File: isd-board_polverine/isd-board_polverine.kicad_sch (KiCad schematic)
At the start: 27 parts, among them J1 BATT, J10 Conn_01x02_Pin, J12 Conn_02x10_Odd_Even, J3 Conn_01x02_Pin, J4 Conn_02x08_Odd_Even, J5 Conn_02x08_Odd_Even, J8 USB_C_Receptacle_PowerOnly_6P, J9 Conn_01x04_Socket, Q1 Q_Dual_NMOS_S1G1D2S2G2D1, U1 DW01A

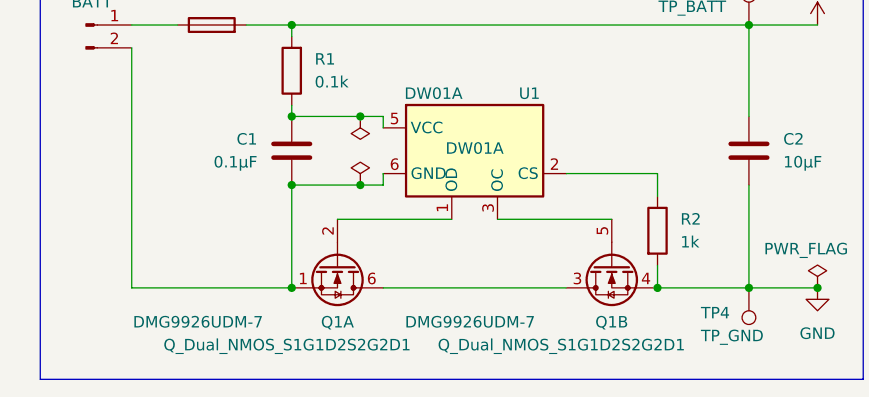
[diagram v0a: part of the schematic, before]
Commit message: update: battery protection circuit (compact placement)
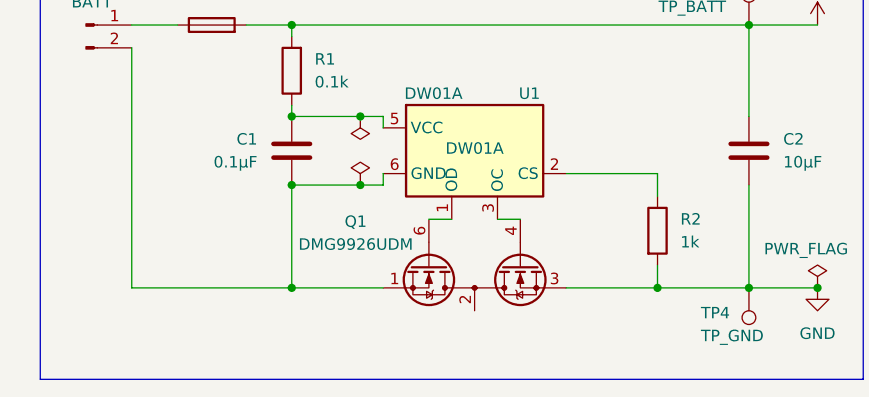
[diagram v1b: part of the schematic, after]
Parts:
- removed Q1: Q_Dual_NMOS_S1G1D2S2G2D1, Package_TO_SOT_SMD:SOT-23-6_Handsoldering, symbol Transistor_FET:Q_Dual_NMOS_S1G1D2S2G2D1
- added Q1: DMG9926UDM, Package_TO_SOT_SMD:SOT-23-6, symbol Transistor_FET:DMG9926UDM
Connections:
- net GND: now also Q1.3 (S2)
- net at U1.1 (OD): now also Q1.6 (G1)
- net at U1.3 (OC): now also Q1.4 (G2)
- net at C1.2, J1.2 (Pin_2), U1.6 (GND): now also Q1.1 (D1)
- new net: Q1.2 (S1/D2), Q1.5 (S1/D2)
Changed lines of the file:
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@@
 	)
 	(junction
-		(at 46.99 152.4)
+		(at 87.63 181.61)
 		(diameter 0)
 		(color 0 0 0 0)
 	)
 	(junction
-		(at 146.05 173.99)
+		(at 46.99 152.4)
 		(diameter 0)
 		(color 0 0 0 0)
 	)
 	(junction
-		(at 139.7 74.93)
+		(at 146.05 173.99)
 		(diameter 0)
 		(color 0 0 0 0)
 	)
 	(junction
-		(at 46.99 181.61)
+		(at 139.7 74.93)
 		(diameter 0)
 		(color 0 0 0 0)
@@
 	)
 	(junction
-		(at 97.79 181.61)
+		(at 46.99 181.61)
 		(diameter 0)
 		(color 0 0 0 0)
 	)
 	(junction
-		(at 62.23 124.46)
+		(at 97.79 181.61)
 		(diameter 0)
 		(color 0 0 0 0)
 	)
 	(junction
-		(at 152.4 107.95)
+		(at 62.23 124.46)
 		(diameter 0)
 		(color 0 0 0 0)
 	)
 	(junction
-		(at 46.99 170.18)
+		(at 152.4 107.95)
 		(diameter 0)
 		(color 0 0 0 0)
 	)
 	(junction
-		(at 87.63 181.61)
+		(at 46.99 170.18)
 		(diameter 0)
 		(color 0 0 0 0)
@@
 	(wire
 		(pts
-			(xy 190.5 83.82) (xy 198.12 83.82)
+			(xy 46.99 181.61) (xy 57.15 181.61)
 		)
 		(stroke
@@
 	(wire
 		(pts
-			(xy 57.15 181.61) (xy 77.47 181.61)
+			(xy 190.5 83.82) (xy 198.12 83.82)
 		)
 		(stroke
@@
 	(wire
 		(pts
-			(xy 69.85 173.99) (xy 82.55 173.99)
-		)
-		(stroke
-			(width 0)
-			(type default)
-		)
-	)
-	(wire
-		(pts
 			(xy 129.54 133.35) (xy 133.35 133.35)
 		)
@@
 	(wire
 		(pts
-			(xy 52.07 173.99) (xy 64.77 173.99)
+			(xy 77.47 181.61) (xy 87.63 181.61)
 		)
 		(stroke
@@
 	(wire
 		(pts
+			(xy 69.85 173.99) (xy 72.39 173.99)
+		)
+		(stroke
+			(width 0)
+			(type default)
+		)
+	)
+	(wire
+		(pts
 			(xy 190.5 86.36) (xy 198.12 86.36)
 		)
@@
 	(wire
 		(pts
+			(xy 62.23 173.99) (xy 64.77 173.99)
+		)
+		(stroke
+			(width 0)
+			(type default)
+		)
+	)
+	(wire
+		(pts
 			(xy 97.79 181.61) (xy 105.41 181.61)
 		)
@@
 	)
 	(symbol
+		(lib_id "Transistor_FET:DMG9926UDM")
+		(at 67.31 181.61 90)
+		(mirror x)
+		(unit 1)
+		(exclude_from_sim no)
+		(in_bom yes)
+		(on_board yes)
+		(dnp no)
+		(property "Reference" "Q1"
+			(at 54.102 174.244 90)
+			(effects
+				(font
+					(size 1.27 1.27)
+				)
+			)
+		)
+		(property "Value" "DMG9926UDM"
+			(at 54.102 176.784 90)
+			(effects
+				(font
+					(size 1.27 1.27)
+				)
+			)
+		)
+		(property "Footprint" "Package_TO_SOT_SMD:SOT-23-6"
+			(at 71.12 184.15 0)
+			(effects
+				(font
+					(size 1.27 1.27)
+					(italic yes)
+				)
+				(justify left)
+				(hide yes)
+			)
+		)
+		(property "Datasheet" "https://www.diodes.com/assets/Datasheets/ds31770.pdf"
+			(at 73.025 184.15 0)
+			(effects
+				(font
+					(size 1.27 1.27)
+				)
+				(justify left)
+				(hide yes)
+			)
+		)
+		(property "Description" "4.2A Id, 20V Vds, Common-Drain, Dual Half Bridge N-Channel MOSFET, 28mOhm Ron, SOT-23-6"
+			(at 67.31 181.61 0)
+			(effects
+				(font
+					(size 1.27 1.27)
+				)
+				(hide yes)
+			)
+		)
+		(pin "5"
+		)
+		(pin "2"
+		)
+		(pin "6"
+		)
+		(pin "3"
+		)
+		(pin "1"
+		)
+		(pin "4"
+		)
+		(instances
+			(project ""
+				(path "/27bbddde-1315-4a7b-91f8-52269d45b0e3"
+					(reference "Q1")
+					(unit 1)
+				)
+			)
+		)
+	)
+	(symbol
 		(lib_id "Device:R")
 		(at 46.99 157.48 180)
@@
 	)
 	(symbol
-		(lib_id "Transistor_FET:Q_Dual_NMOS_S1G1D2S2G2D1")
-		(at 52.07 179.07 270)
-		(unit 1)
-		(exclude_from_sim no)
-		(in_bom yes)
-		(on_board yes)
-		(dnp no)
-		(property "Reference" "Q1"
-			(at 52.07 185.42 90)
-			(effects
-				(font
-					(size 1.27 1.27)
-				)
-			)
-		)
-		(property "Value" "Q_Dual_NMOS_S1G1D2S2G2D1"
-			(at 46.482 187.96 90)
-			(effects
-				(font
-					(size 1.27 1.27)
-				)
-			)
-		)
-		(property "Footprint" "Package_TO_SOT_SMD:SOT-23-6_Handsoldering"
-			(at 52.07 184.15 0)
-			(effects
-				(font
-					(size 1.27 1.27)
-				)
-				(hide yes)
-			)
-		)
-		(property "Datasheet" "https://www.mouser.fi/datasheet/3/175/1/ds31770.pdf"
-			(at 52.07 184.15 0)
-			(effects
-				(font
-					(size 1.27 1.27)
-				)
-				(hide yes)
-			)
-		)
-		(property "Description" "Dual NMOS transistor, 6 pin package"
-			(at 52.07 179.07 0)
-			(effects
-				(font
-					(size 1.27 1.27)
-				)
-				(hide yes)
-			)
-		)
-		(property "MPN" "DMG9926UDM-7"
-			(at 36.576 185.42 90)
-			(effects
-				(font
-					(size 1.27 1.27)
-				)
-			)
-		)
-		(pin "1"
-		)
-		(pin "6"
-		)
-		(pin "4"
-		)
-		(pin "2"
-		)
-		(pin "5"
-		)
-		(pin "3"
-		)
-		(instances
-			(project ""
-				(path "/27bbddde-1315-4a7b-91f8-52269d45b0e3"
-					(reference "Q1")
-					(unit 1)
-				)
-			)
-		)
-	)
-	(symbol
 		(lib_id "Device:C")
 		(at 97.79 166.37 0)
@@
 				)
 			)
-		)
-	)
-	(symbol
-		(lib_id "Transistor_FET:Q_Dual_NMOS_S1G1D2S2G2D1")
-		(at 82.55 179.07 90)
-		(mirror x)
-		(unit 2)
-		(exclude_from_sim no)
-		(in_bom yes)
-		(on_board yes)
-		(dnp no)
-		(property "Reference" "Q1"
-			(at 82.55 185.42 90)
-			(effects
-				(font
-					(size 1.27 1.27)
-				)
-			)
-		)
-		(property "Value" "Q_Dual_NMOS_S1G1D2S2G2D1"
-			(at 76.962 187.96 90)
-			(effects
-				(font
-					(size 1.27 1.27)
-				)
-			)
-		)
-		(property "Footprint" "Package_TO_SOT_SMD:SOT-23-6_Handsoldering"
-			(at 82.55 184.15 0)
-			(effects
-				(font
-					(size 1.27 1.27)
-				)
-				(hide yes)
-			)
-		)
-		(property "Datasheet" "https://www.mouser.fi/datasheet/3/175/1/ds31770.pdf"
-			(at 82.55 184.15 0)
-			(effects
-				(font
-					(size 1.27 1.27)
-				)
-				(hide yes)
-			)
-		)
-		(property "Description" "Dual NMOS transistor, 6 pin package"
-			(at 82.55 179.07 0)
-			(effects
-				(font
-					(size 1.27 1.27)
-				)
-				(hide yes)
-			)
-		)
-		(property "MPN" "DMG9926UDM-7"
-			(at 66.802 185.42 90)
-			(effects
-				(font
-					(size 1.27 1.27)
-				)
-			)
-		)
-		(pin "1"
-		)
-		(pin "6"
-		)
-		(pin "4"
-		)
-		(pin "2"
-		)
-		(pin "5"
-		)
-		(pin "3"
-		)
-		(instances
-			(project ""
-				(path "/27bbddde-1315-4a7b-91f8-52269d45b0e3"
-					(reference "Q1")
-					(unit 2)
-				)
-			)

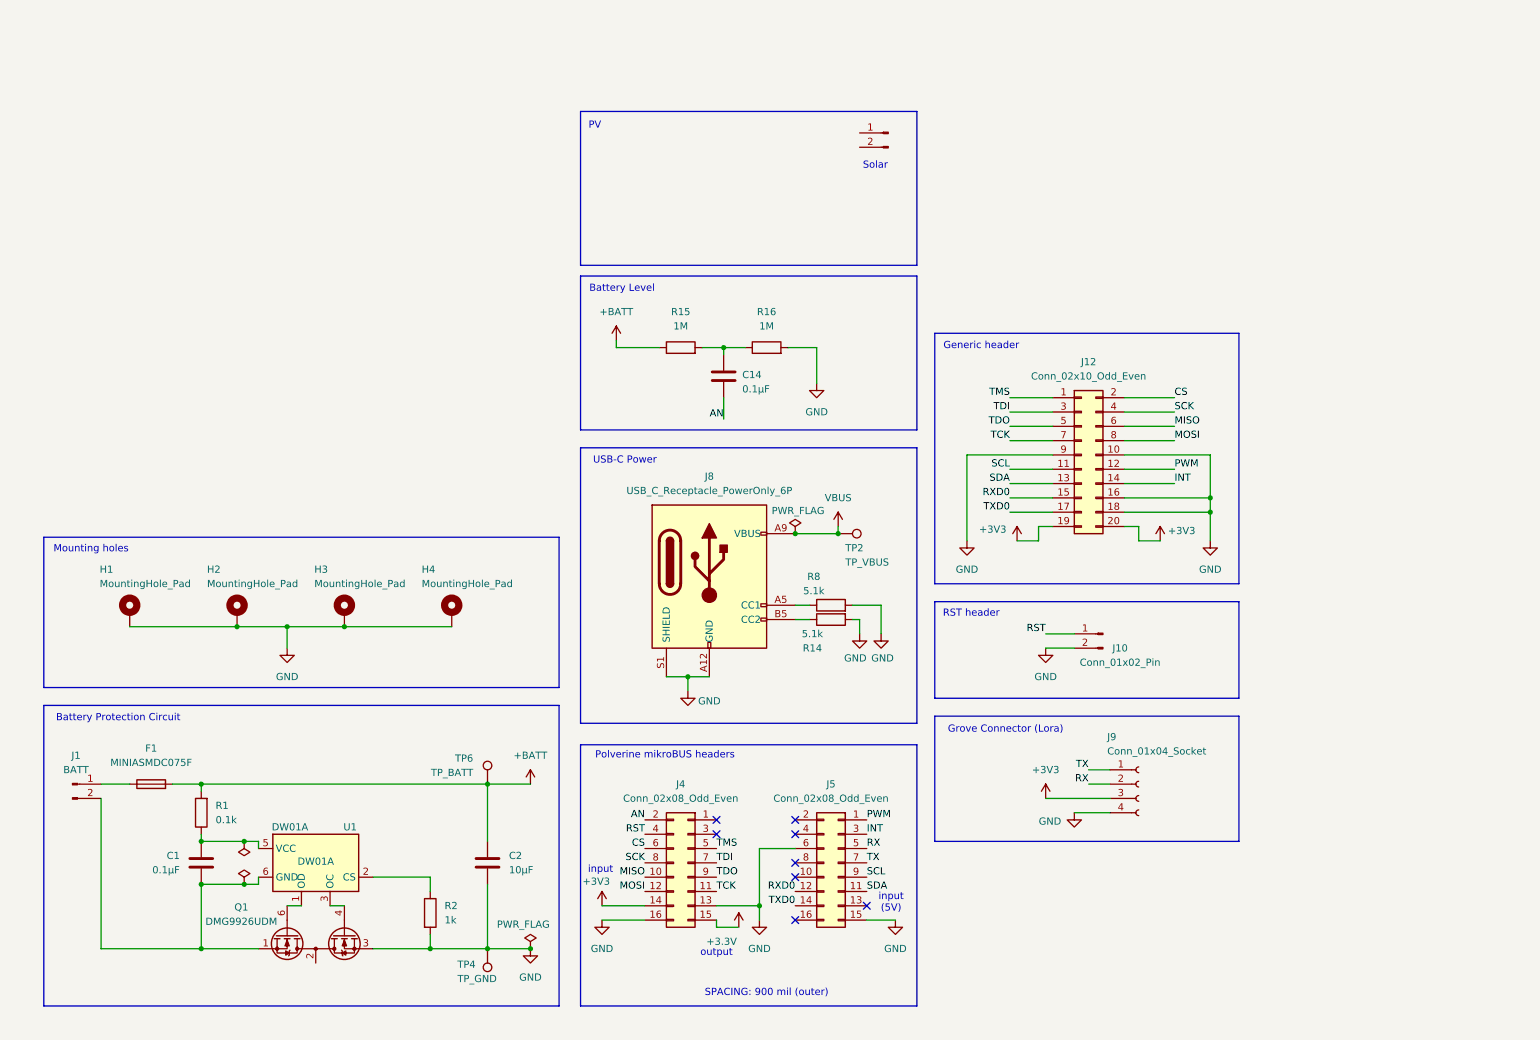
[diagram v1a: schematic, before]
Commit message: update: dual-socket sch/pcb (polverine socket, dfr1117 socket, grove-conn, zif-conn (bmv080), lga 3x3mm (bme690), b5b-zr (sps30))
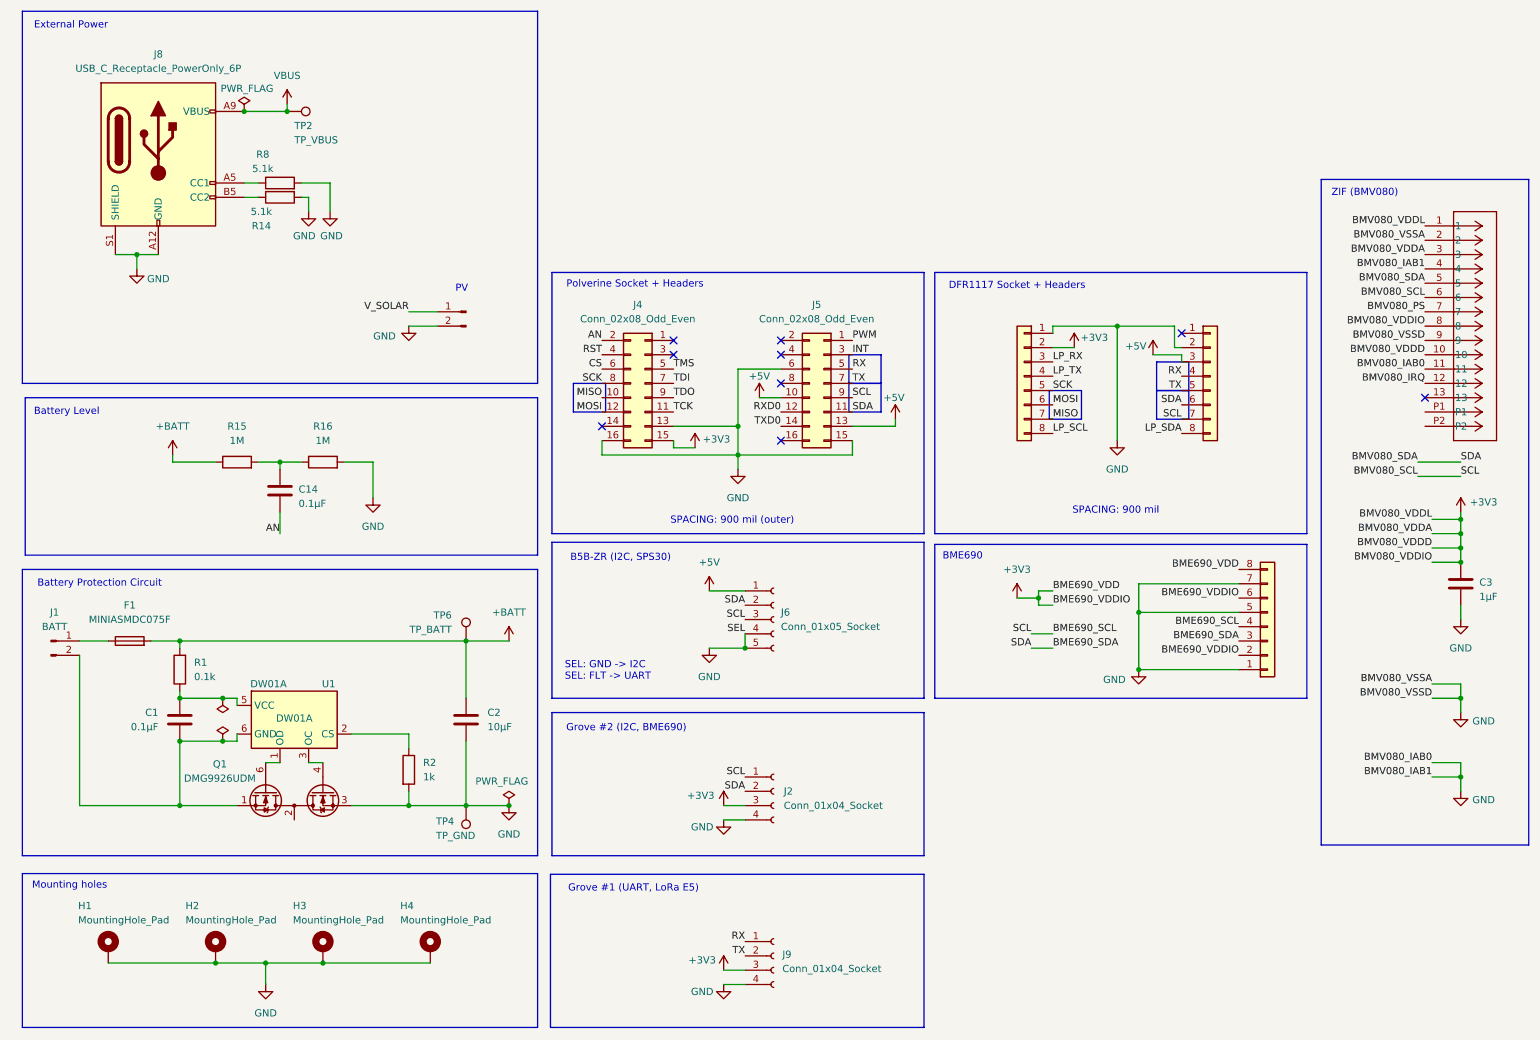
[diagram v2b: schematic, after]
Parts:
- removed J10: Conn_01x02_Pin, Connector_PinHeader_2.54mm:PinHeader_1x02_P2.54mm_Vertical, symbol Connector:Conn_01x02_Pin
- removed J12: Conn_02x10_Odd_Even, Connector_PinHeader_2.54mm:PinHeader_2x10_P2.54mm_Vertical, symbol Connector_Generic:Conn_02x10_Odd_Even
- added C3: 1µF, Capacitor_SMD:C_0805_2012Metric_Pad1.18x1.45mm_HandSolder, symbol Device:C
- added J10, J7: Conn_01x08, Connector_PinSocket_2.54mm:PinSocket_1x08_P2.54mm_Vertical, symbol Connector_Generic:Conn_01x08
- added J11: Conn_01x08, Package_LGA:Bosch_LGA-8_3x3mm_P0.8mm_ClockwisePinNumbering, symbol Connector_Generic:Conn_01x08
- added J12: 5035661302, CON_5035661302_MOL, symbol CON_5035661302_MOL:5035661302
- added J2: Conn_01x04_Socket, Connector:NS-Tech_Grove_1x04_P2mm_Vertical, symbol Connector:Conn_01x04_Socket
- added J6: Conn_01x05_Socket, Connector_JST:JST_ZH_B5B-ZR_1x05_P1.50mm_Vertical, symbol Connector:Conn_01x05_Socket
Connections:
- net +3V3: now also J4.15 (Pin_15), C3.1, J10.2 (Pin_2), J11.2 (Pin_2), J11.6 (Pin_6), J11.8 (Pin_8), J12.1, J12.10, J12.3, J12.8, J2.3 (Pin_3); no longer J4.14 (Pin_14)
- net GND: now also J3.2 (Pin_2), C3.2, J10.1 (Pin_1), J11.1 (Pin_1), J11.5 (Pin_5), J11.7 (Pin_7), J12.11, J12.2, J12.4, J12.9, J2.4 (Pin_4), J6.4 (Pin_4), J6.5 (Pin_5), J7.2 (Pin_2)
- net MISO: now also J10.7 (Pin_7)
- net MOSI: now also J10.6 (Pin_6)
- net RX: now also J9.1 (Pin_1), J7.4 (Pin_4); no longer J9.2 (Pin_2)
- net SCK: now also J10.5 (Pin_5)
- net TX: now also J9.2 (Pin_2), J7.5 (Pin_5); no longer J9.1 (Pin_1)
- net V_SOLAR: now reaches J3.1 (Pin_1)
- net +5V: now reaches J5.10 (Pin_10)
- net +5V: now also J5.13 (Pin_13), J6.1 (Pin_1), J7.3 (Pin_3)
- net SCL renamed BME690_SCL
- net BME690_SCL: now also J11.4 (Pin_4), J12.6, J2.1 (Pin_1), J6.3 (Pin_3), J7.7 (Pin_7)
- net SDA renamed BME690_SDA
- net BME690_SDA: now also J11.3 (Pin_3), J12.5, J2.2 (Pin_2), J6.2 (Pin_2), J7.6 (Pin_6)
- new net BMV080_IRQ: J12.12
- new net BMV080_PS: J12.7
- new net LP_RX: J10.3 (Pin_3)
- new net LP_SCL: J10.8 (Pin_8)
- new net LP_SDA: J7.8 (Pin_8)
- new net LP_TX: J10.4 (Pin_4)
- no-connect marks 8 -> 9
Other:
- note added: "B5B-ZR (I2C, SPS30)"
- note added: "BME690"
- note added: "DFR1117 Socket + Headers"
- note added: "External Power"
- note added: "Grove #1 (UART, LoRa E5)"
- note added: "Grove #2 (I2C, BME690)"
- note added: "Polverine Socket + Headers"
- note added: "SEL: GND -> I2C SEL: FLT -> UART"
- note added: "SPACING: 900 mil"
- note added: "ZIF (BMV080)"
- note removed: "Generic header"
- note removed: "Grove Connector (Lora)"
- note removed: "Polverine mikroBUS headers"
- note removed: "RST header"
- note removed: "Solar"
- note removed: "USB-C Power"
- note removed: "input"
- note removed: "input (5V)"
- note removed: "output"
- moved on the sheet: C1, C14, C2, F1, H1, H2, H3, H4, J1, J4, J5, J8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

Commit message: Added resistor values to MPPT and connection to Battery protection
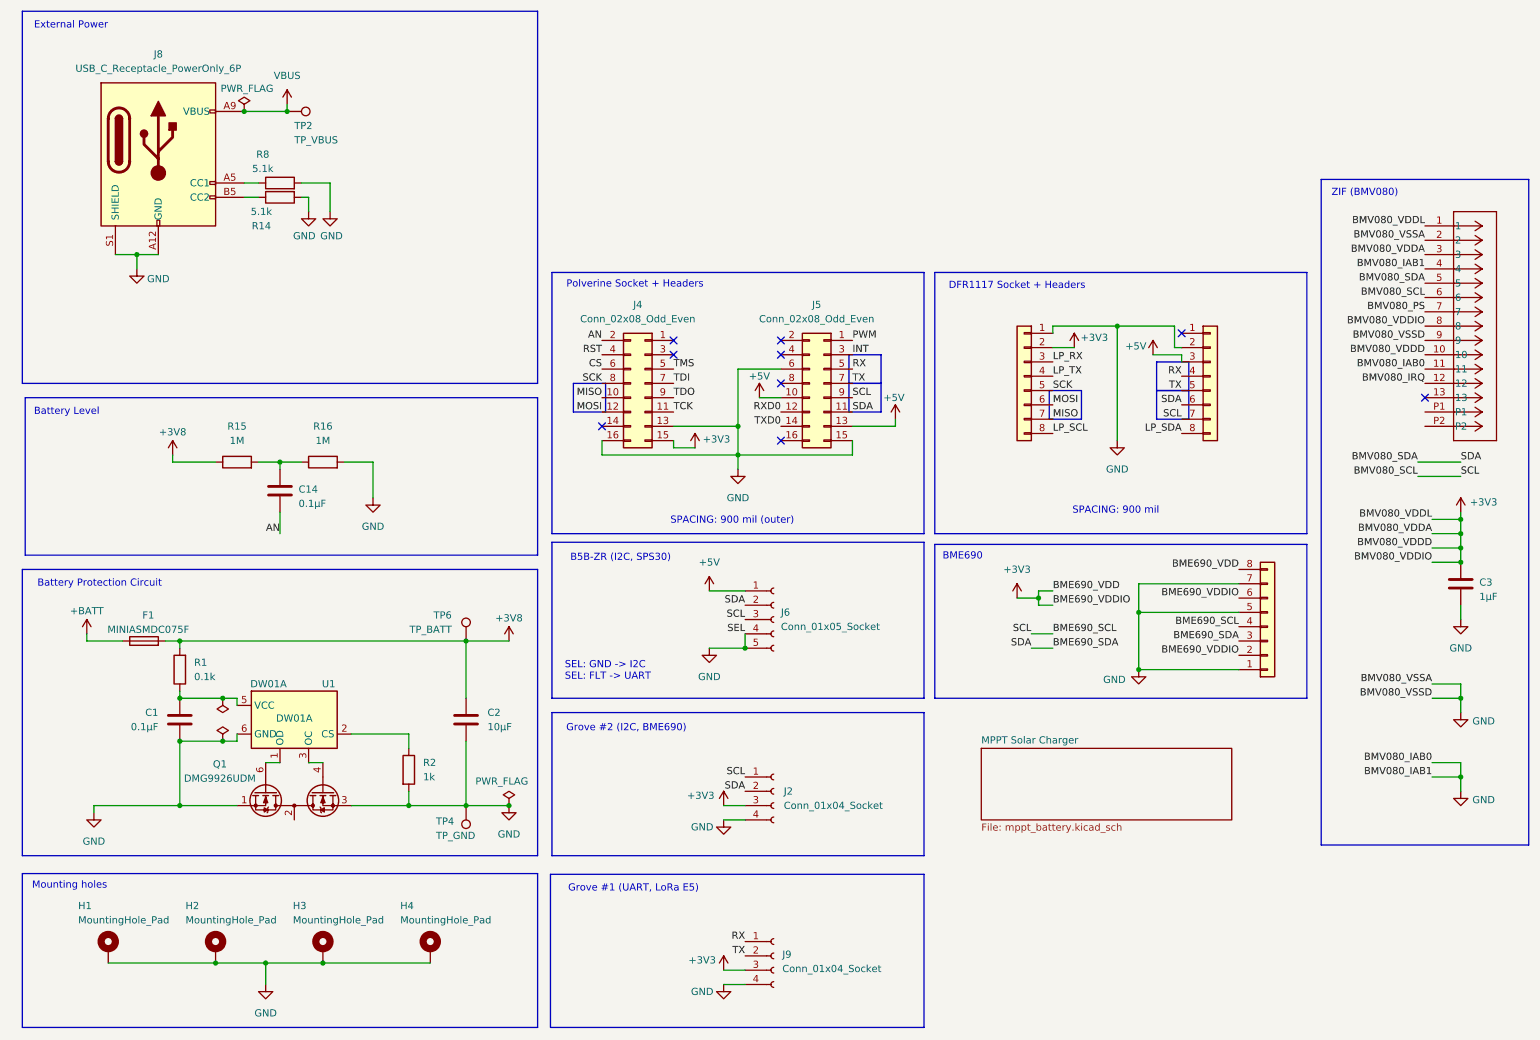
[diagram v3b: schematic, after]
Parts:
- removed J1: BATT, Connector_JST:JST_PH_S2B-PH-K_1x02_P2.00mm_Horizontal, symbol Connector:Conn_01x02_Pin
- removed J3: Conn_01x02_Pin, Connector_JST:JST_PH_S2B-PH-K_1x02_P2.00mm_Horizontal, symbol Connector:Conn_01x02_Pin
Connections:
- net +BATT: now also F1.1; no longer C2.1, F1.2, R1.2, R15.1, TP6.1
- net GND: now also C1.2, Q1.1 (D1), U1.6 (GND)
- new net +3V8: C2.1, F1.2, R1.2, R15.1, TP6.1
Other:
- added sheet MPPT Solar Charger (mppt_battery.kicad_sch)
- note removed: "PV"
- moved on the sheet: F1
